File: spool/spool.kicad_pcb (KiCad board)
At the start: 4 copper layers, 80 x 95 mm, 135 parts, among them J1 USB_B_Micro, J13 Conn_02x10_Counter_Clockwise, J14 Conn_01x07, J2 SWD, J3 Switch_1, J4 Switch_1, J5 Switch_1, J6 Switch_2, J7 Conn_01x02, J8 Conn_01x08, M1 Motor_DC, Q1 AO3400A, Q101 Q_NMOS_GSD, Q2 2N7002, SW1 USB_BOOT, SW2 RESET, SW3 SW_Push_DPDT, SW4 SW_Coded_SH-7010, SW5 SW_Push_DPDT, U1 TPS63070RNMR, U10 HT75xx-1-SOT89, U101 MMA8451QR1, U102 INA219AxDCN, U103 DY-ITR8402, U104 DY-ITR8402, U11 TPL0401B-10-Q1, U12 BS612, U14 PCF8563T, U3 AS5600-ASOT, U6 DRV8871DDA, U7 W25Q128JVS, U8 RP2040, U9 BS612, Y1 Crystal_GND24, Y2 Crystal

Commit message: Tidy up
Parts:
- L101: footprint Connector_JST:JST_XA_B02B-XASK-1-A_1x02_P2.50mm_Vertical -> Connector_JST:JST_XA_B03B-XASK-1-A_1x03_P2.50mm_Vertical
- R103: value R_Shunt -> 100mΩ
- moved D101 6.75 mm to (-25.7, -30.6), turned to -90 degrees
- moved Q101 4.59 mm to (-16.7, -28.3)
- moved R104 2.62 mm to (31.4, -3.52)
- moved L101 1.91 mm to (-20.2, -38.3), turned to -90 degrees
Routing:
- net Net-(D101-A): track 6.80 -> 17.0 mm
- net SDA: track 118.9 -> 124.8 mm
- net +12V: track 27.4 -> 31.4 mm
- net RELEASE: track 68.9 -> 65.6 mm
- net SCL: track 122.7 -> 124.7 mm
- net GND: track 80.0 -> 78.1 mm, vias 79 -> 80
- net +3V3: track 61.3 -> 61.6 mm, vias 29 -> 47
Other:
- outline, holes or cut-outs redrawn
- board text added: "Magnet Release"
- board text added: "Motor"

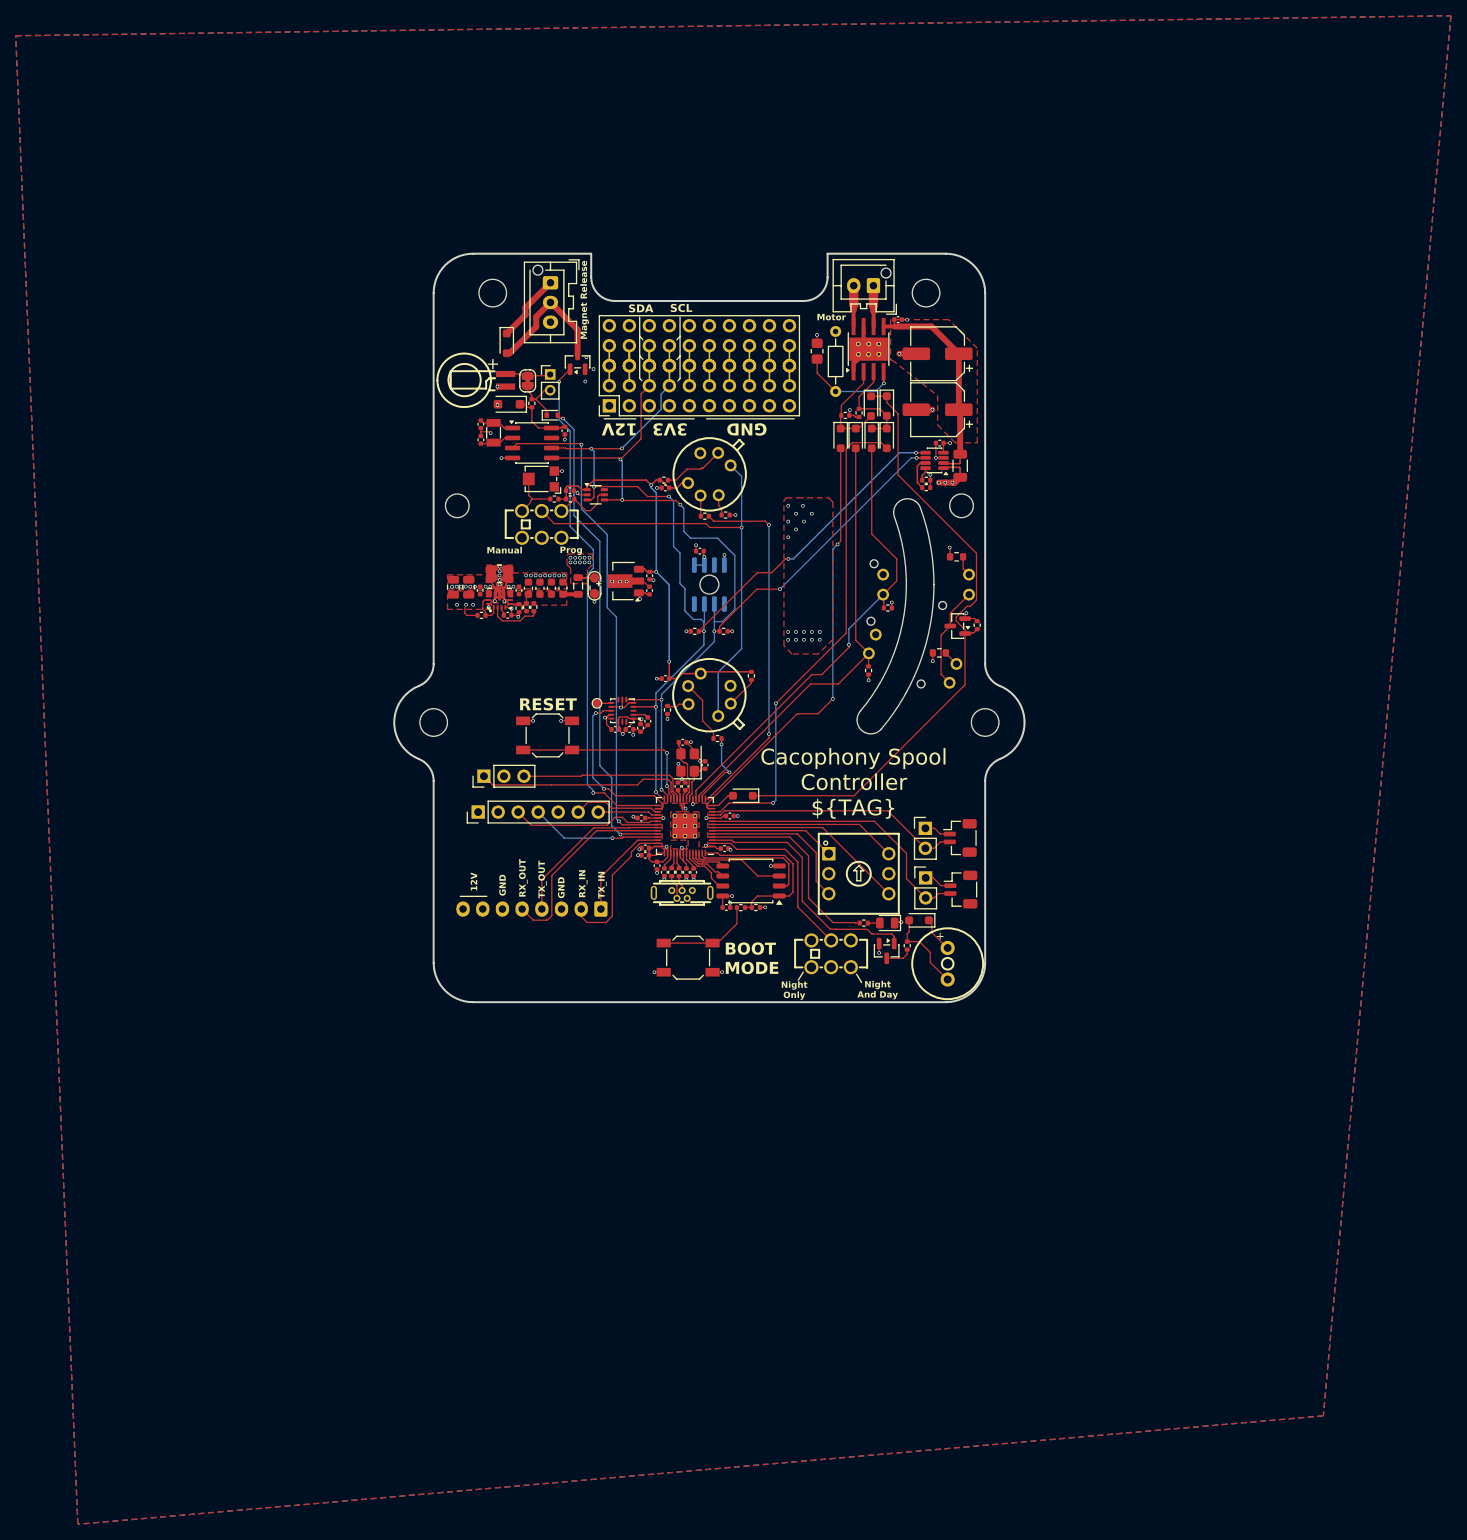
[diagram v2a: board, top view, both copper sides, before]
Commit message: Add servo, more inputs and update board layout
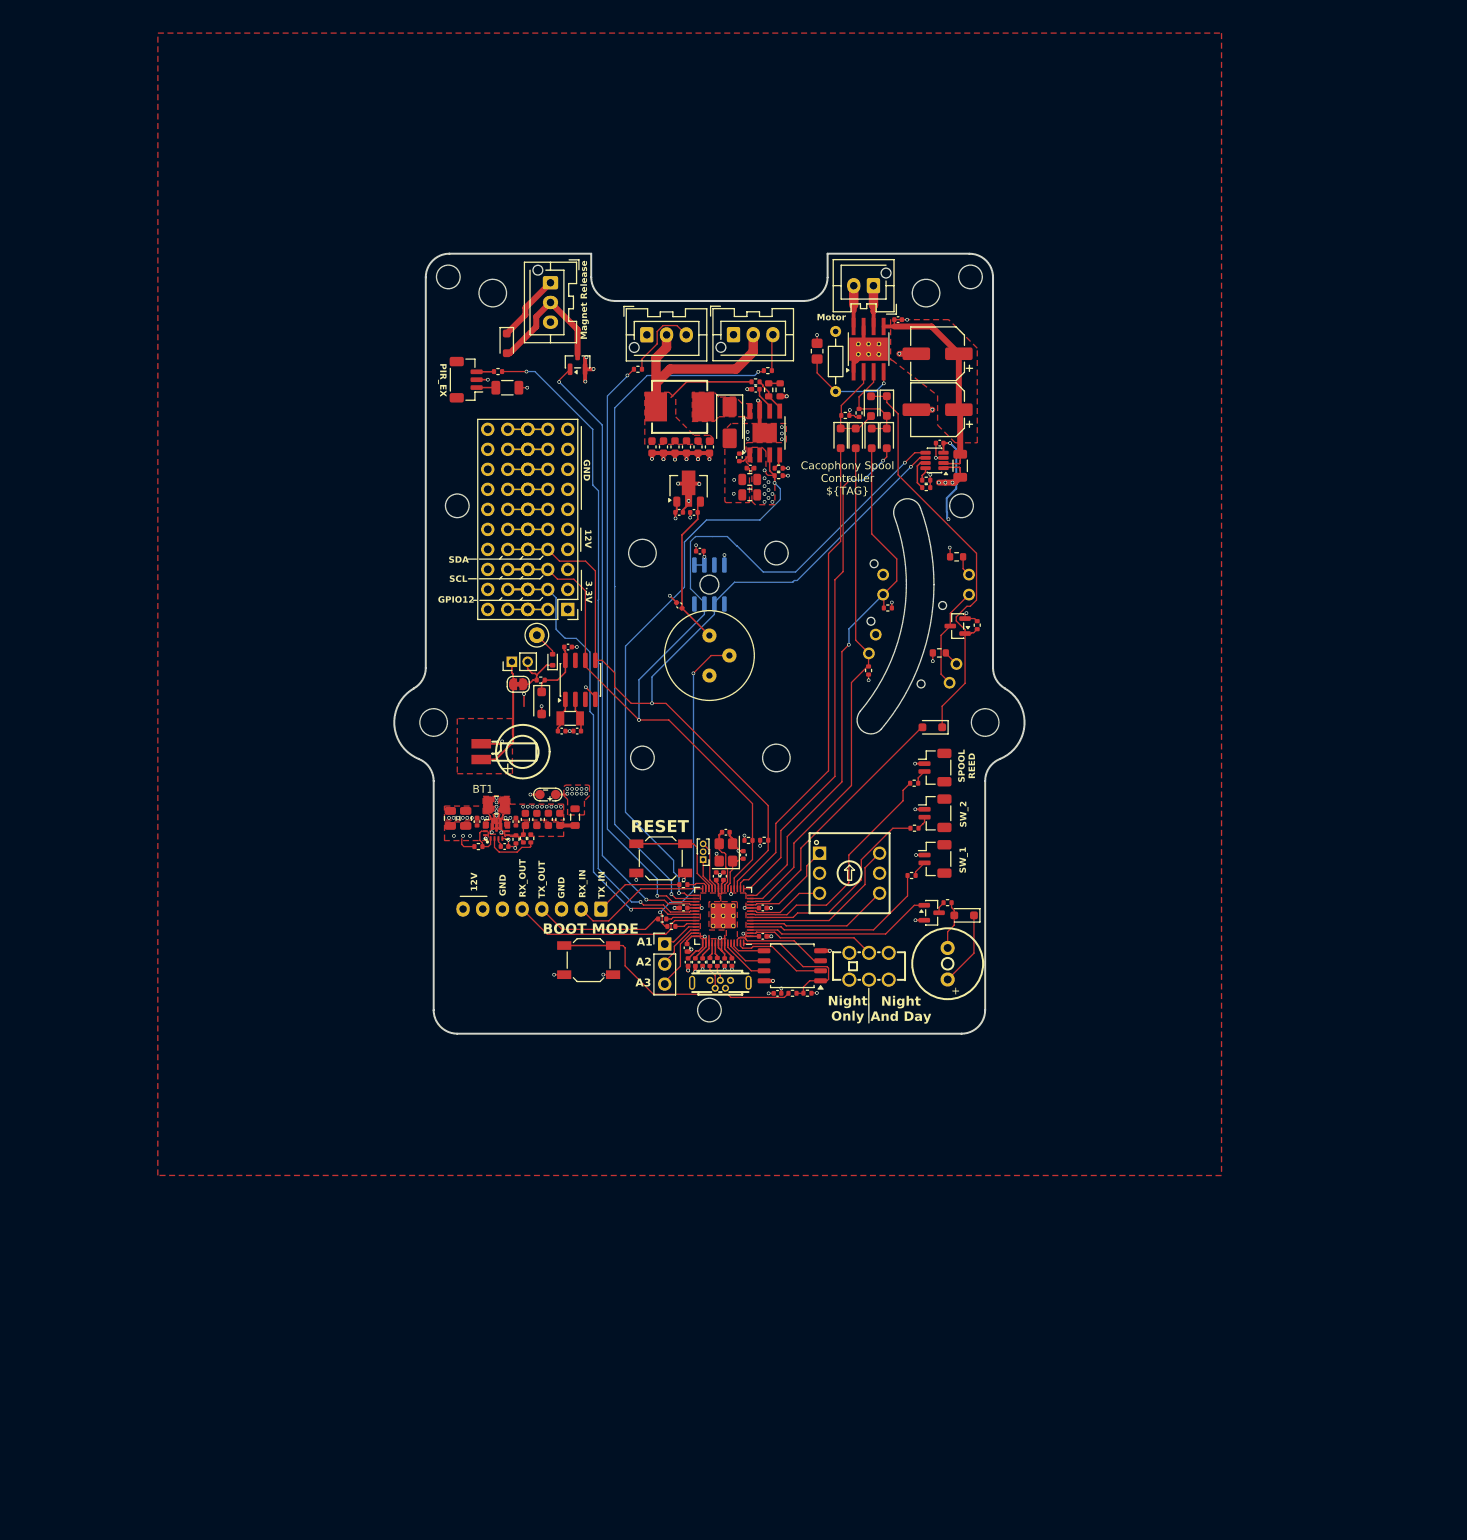
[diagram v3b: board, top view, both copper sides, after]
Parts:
- removed C101, C102: 100n, Capacitor_SMD:C_0402_1005Metric
- removed C103, C105: 2.2uF, Capacitor_SMD:C_0402_1005Metric
- removed D1: LED, LED_SMD:LED_0805_2012Metric
- removed J14: Conn_01x07, Connector_PinHeader_2.54mm:PinHeader_1x07_P2.54mm_Vertical
- removed R24, R30: 1k, Resistor_SMD:R_0402_1005Metric
- removed R28, R29: 10k, Resistor_SMD:R_0402_1005Metric
- removed RV1: 10k, Potentiometer_SMD:Potentiometer_Bourns_TC33X_Vertical
- removed SW3: SW_Push_DPDT, cacophony-library:SW-TH_K3-2235D-F1
- removed TP101: TestPoint, cacophony-library:TP_PAD
- removed U101: MMA8451QR1, cacophony-library:QFN-16_L3.0-W3.0-P0.50-TL_FXOS8700CQR1
- removed U11: TPL0401B-10-Q1, Package_TO_SOT_SMD:Texas_R-PDSO-G6
- removed U12: BS612, cacophony-library:SENSORM-TH_BS612
- added C36: 22uF, Capacitor_SMD:C_0603_1608Metric, F.Cu at (0.01, -17.5)
- added C37: 22nF, Capacitor_SMD:C_0402_1005Metric, F.Cu at (5.88, -24.8)
- added C38: 100nF, Capacitor_SMD:C_0402_1005Metric, F.Cu at (3.80, -16.1)
- added C40: 100n, Capacitor_SMD:C_0402_1005Metric, F.Cu at (-3.82, 2.64)
- added C46: 22uF, Capacitor_SMD:C_0603_1608Metric, F.Cu at (-1.45, -17.5)
- added C47: 22uF, Capacitor_SMD:C_0603_1608Metric, F.Cu at (-2.91, -17.5)
- added C48: 22uF, Capacitor_SMD:C_0603_1608Metric, F.Cu at (-4.37, -17.5)
- added C49: 22uF, Capacitor_SMD:C_0603_1608Metric, F.Cu at (-5.83, -17.5)
- added C50: 22uF, Capacitor_SMD:C_0603_1608Metric, F.Cu at (-7.29, -17.5)
- added D17: D_Shockley, Diode_SMD:D_SMA, F.Cu at (2.57, -20.6)
- added H10: MountingHole, cacophony-library:MountingHole_3.5mm_M3, F.Cu at (8.50, 22.0)
- added H11: MountingHole, cacophony-library:3.0mm_key_hole, F.Cu at (-33.1, -39.1)
- added H12: MountingHole, cacophony-library:3.0mm_key_hole, F.Cu at (33.1, -39.1)
- added H13: MountingHole, cacophony-library:3.0mm_key_hole, F.Cu at (0.00, 54.0)
- added H7: MountingHole, cacophony-library:3.0mm_key_hole, F.Cu at (-8.50, 22.0)
- added H8: MountingHole, cacophony-library:3.0mm_key_hole, F.Cu at (8.50, -4.00)
- added H9: MountingHole, cacophony-library:MountingHole_3.5mm_M3, F.Cu at (-8.50, -4.00)
- added J9: Switch_2, Connector_JST:JST_SH_BM02B-SRSS-TB_1x02-1MP_P1.00mm_Vertical, F.Cu at (28.6, 23.2)
- added L2: 4.7uH, cacophony-library:IND-SMD_L7.0-W6.6, F.Cu at (-3.78, -22.6)
- added M2: Servo, Connector_JST:JST_XA_B03B-XASK-1-A_1x03_P2.50mm_Vertical, F.Cu at (-7.94, -31.7)
- added M3: Servo, Connector_JST:JST_XA_B03B-XASK-1-A_1x03_P2.50mm_Vertical, F.Cu at (3.06, -31.7)
- added R34: 1k, Resistor_SMD:R_0402_1005Metric, F.Cu at (-9.07, -27.3)
- added R35: 1k, Resistor_SMD:R_0402_1005Metric, F.Cu at (7.42, -27.2)
- added R37: 1k, Resistor_SMD:R_0402_1005Metric, F.Cu at (-4.83, 43.4)
- added R38: 1k, Resistor_SMD:R_0402_1005Metric, F.Cu at (25.7, 36.9)
- added R39: 1k, Resistor_SMD:R_0402_1005Metric, F.Cu at (26.0, 25.2)
- added R40: 1k, Resistor_SMD:R_0402_1005Metric, F.Cu at (26.0, 30.9)
- added R41: 1k, Resistor_SMD:R_0402_1005Metric, F.Cu at (-26.8, -27.0)
- added R42: 1k, Resistor_SMD:R_1206_3216Metric, F.Cu at (-25.6, -25.0)
- added R43: 1k, Resistor_SMD:R_0402_1005Metric, F.Cu at (-5.99, 42.4)
- added R44: 1k, Resistor_SMD:R_0402_1005Metric, F.Cu at (-3.30, 38.1)
- added TP2: TestPoint, TestPoint:TestPoint_Loop_D1.80mm_Drill1.0mm_Beaded, F.Cu at (-21.9, 6.42)
- added U2: PA_PIR, cacophony-library:PA_PIR, F.Cu at (0.00, 9.00)
- C27: value 100n -> 2.2uF
- C28, C29: value 100n -> 22uF; footprint Capacitor_SMD:C_0402_1005Metric -> Capacitor_SMD:C_0805_2012Metric
- J2: footprint Connector_PinHeader_2.54mm:PinHeader_1x03_P2.54mm_Vertical -> Connector_PinHeader_1.00mm:PinHeader_1x03_P1.00mm_Vertical
- J3: value Switch_1 -> Conn_01x03; footprint Connector_PinHeader_2.54mm:PinHeader_1x02_P2.54mm_Vertical -> Connector_JST:JST_SH_BM03B-SRSS-TB_1x03-1MP_P1.00mm_Vertical
- J4, J6: footprint cacophony-library:JST_SH_BM02B-SRSS-TB_1x02-1MP_P1.00mm_Vertical -> Connector_JST:JST_SH_BM02B-SRSS-TB_1x02-1MP_P1.00mm_Vertical
- J5: value Switch_1 -> Conn_01x03; footprint Connector_PinHeader_2.54mm:PinHeader_1x02_P2.54mm_Vertical -> Connector_PinHeader_2.54mm:PinHeader_1x03_P2.54mm_Vertical
- L101: footprint Connector_JST:JST_XA_B03B-XASK-1-A_1x03_P2.50mm_Vertical -> cacophony-library:JST_XA_B03B_2_Pin
- R22: value 10k -> 47k
- R25: value 10k -> 100k
- R26: value 1k -> 560; footprint Resistor_SMD:R_0402_1005Metric -> Resistor_SMD:R_0603_1608Metric
- R27: value 10k -> 680; footprint Resistor_SMD:R_0402_1005Metric -> Resistor_SMD:R_0603_1608Metric
- SW1, SW2: footprint Button_Switch_SMD:SW_SPST_SKQG_WithStem -> cacophony-library:SW_SPST_SKQG_WithStem
- U9: value BS612 -> LMR14050S; footprint cacophony-library:SENSORM-TH_BS612 -> Package_SO:TI_SO-PowerPAD-8
- moved J3 86.0 mm to (-30.9, -26.0), turned to 90 degrees
- moved BT1 47.2 mm to (-28.8, 21.2), turned to 180 degrees
- moved R26 44.7 mm to (7.52, -24.7), turned to 90 degrees
- moved C31 40.3 mm to (-18.8, 18.6), turned to 0 degrees
- moved C32 38.9 mm to (-16.8, 18.6), turned to 180 degrees
- moved JP1 38.5 mm to (-24.3, 12.7), turned to 0 degrees
- moved D2 38.1 mm to (-21.3, 15.0), turned to -90 degrees
- moved Y2 37.5 mm to (-17.7, 17.0), turned to 0 degrees
- moved J7 36.8 mm to (-25.1, 9.79), turned to 90 degrees
- moved J5 36.2 mm to (-5.67, 45.6)
- moved R32 35.1 mm to (-21.4, 12.1), turned to 180 degrees
- moved U9 34.0 mm to (7.01, -19.2), turned to 90 degrees
- moved R25 32.9 mm to (8.79, -13.8), turned to 180 degrees
- moved D3 31.0 mm to (-19.9, 9.54), turned to 90 degrees
- moved U14 30.7 mm to (-16.4, 12.1), turned to 90 degrees
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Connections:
- C27 pad 1: +3V3_Lin -> +12V
- C28 pad 1: +3V3_Lin -> +12V
- C29 pad 1: +3V3_Lin -> +12V
- D3 pad 2: RTC_BAT_SENSE -> /RTC_BAT_SENSE
- D4 pad 2: Net-(D4-A) -> H_IN2
- D5 pad 2: Net-(D10-K) -> H_IN1
- D6 pad 2: Net-(D6-A) -> /EN_PHOTO_PHY
- D7 pad 1: Net-(D4-A) -> Net-(D7-K)
- D8 pad 1: Net-(D4-A) -> Net-(D7-K)
- J13 pad 1: +12V -> +3V3
- J13 pad 3: +12V -> +3V3
- J13 pad 4: unconnected-(J13-Pin_4-Pad4) -> GPIO_12
- J13 pad 6: SDA -> SCL
- J13 pad 7: +3V3 -> +12V
- J13 pad 8: SCL -> SDA
- J13 pad 9: +3V3 -> +12V
- J3 pad 1: GND -> /EX_PIR_POWER
- J3 pad 2: SWITCH_1 -> GND
- J5 pad 1: GND -> /ADC1
- J5 pad 2: SWITCH_2 -> /ADC2
- R10 pad 1: Net-(D10-K) -> H_IN1
- R12 pad 1: Net-(D4-A) -> H_IN2
- R22 pad 1: +3V3_Lin -> Net-(U9-RT/SYNC)
- R22 pad 2: Net-(U9-OEN) -> GND
- R23 pad 1: /PIR_SENS_POT_MANUAL -> +6V
- R23 pad 2: +3V3_Lin -> Net-(U9-FB)
- R25 pad 2: Net-(U9-ONTIME) -> EN_6V
- R26 pad 1: PIR_1 -> Net-(U9-FB)
- R26 pad 2: Net-(U9-REL) -> Net-(R26-Pad2)
- R27 pad 1: /PIR_SENS_POT_PROG -> Net-(R26-Pad2)
- R27 pad 2: +3V3_Lin -> GND
- U14 pad 3: ~{RTC_INT} -> unconnected-(U14-~{INT}-Pad3)
- U6 pad 2: Net-(D4-A) -> Net-(D7-K)
- U8 pad 11: SWITCH_2 -> R_ENC_1
- U8 pad 12: H_IN1 -> /EN_PHOTO_PHY
- U8 pad 13: H_IN2 -> PHOTO_RESET_OUT
- U8 pad 14: Net-(D6-A) -> PHOTO_HOME_OUT
- U8 pad 15: PIR_2 -> H_IN1
- U8 pad 16: PIR_1 -> H_IN2
- U8 pad 17: PHOTO_RESET_OUT -> SDA
- U8 pad 18: PHOTO_HOME_OUT -> SCL
- U8 pad 27: SDA -> /RP2040_TX_IN_PHY
- U8 pad 28: SCL -> RP2040_RX_IN
- U8 pad 29: RELEASE -> EN_6V
- U8 pad 30: Accel INT1 -> /SERVO_1_PHY
- U8 pad 31: GPIO_20 -> /SERVO_2_PHY
- U8 pad 32: GPIO_21 -> RELEASE
- U8 pad 34: GPIO_34 -> /PIR_EX_PHY
- U8 pad 35: ~{RTC_INT} -> GPIO_12
- U8 pad 36: RP2040_TX_OUT -> /RP2040_TX_OUT_PHY
- U8 pad 38: RTC_BAT_SENSE -> /APIR_PHY
- U8 pad 39: GPIO_27 -> /ADC1
- U8 pad 4: LED_1_PHY -> /SW_1_PHY
- U8 pad 40: RP2040_TX_IN -> /ADC2
- U8 pad 41: RP2040_RX_IN -> /ADC3
- U8 pad 5: R_ENC_4 -> R_ENC_2
- U8 pad 6: R_ENC_1 -> R_ENC_8
- U8 pad 7: R_ENC_2 -> /SW_2_PHY
- U8 pad 8: R_ENC_8 -> /SPOOL_REED_PHY
- U8 pad 9: SWITCH_1 -> R_ENC_4
- U9 pad 1: PIR_SENS_POT -> Net-(U9-Boot)
- U9 pad 2: Net-(U9-OEN) -> +12V
- U9 pad 3: GND -> EN_6V
- U9 pad 4: +3V3_Lin -> Net-(U9-RT/SYNC)
- U9 pad 5: Net-(U9-REL) -> Net-(U9-FB)
- U9 pad 6: Net-(U9-ONTIME) -> Net-(U9-SS)
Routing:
- net /SERVO_1_PHY: track 0.00 -> 88.9 mm, vias 0 -> 2
- net /PIR_EX_PHY: track 0.00 -> 85.4 mm, vias 0 -> 2
- net /SERVO_2_PHY: track 0.00 -> 76.1 mm, vias 0 -> 2
- net EN_6V: track 0.00 -> 73.4 mm, vias 0 -> 2
- net ~{RTC_INT}: track 64.0 -> 0.00 mm, vias 2 -> 0
- net RTC_BAT_SENSE: track 61.5 -> 0.00 mm, vias 2 -> 0
- net PIR_SENS_POT: track 59.9 -> 0.00 mm, vias 1 -> 0
- net GPIO_12: track 0.00 -> 54.5 mm, vias 0 -> 1
- net PIR_2: track 46.4 -> 0.00 mm, vias 2 -> 0
- net APIR: track 0.00 -> 40.8 mm, vias 0 -> 2
- net +6V: track 0.00 -> 39.9 mm
- net +3V3_Lin: track 58.2 -> 19.4 mm, vias 3 -> 0
- net SWITCH_1: track 36.4 -> 2.07 mm
- net /EN_PHOTO_PHY: track 0.00 -> 32.6 mm
- net SWITCH_2: track 32.7 -> 1.72 mm
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- added copper zone on F.Cu, net +6V
- added copper zone on F.Cu, net /SW_6V
- removed copper zone on B.Cu, net GND
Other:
- board size 80 x 95 mm -> 80 x 99 mm
- board text added: "3.3V"
- board text added: "A1"
- board text added: "A2"
- board text added: "A3"
- board text added: "GPIO12"
- board text added: "PIR_EX"
- board text added: "SPOOL REED"
- board text added: "SW_1"
- board text added: "SW_2"
- board text removed: "3V3"
- board text removed: "Manual"
- board text removed: "Prog"

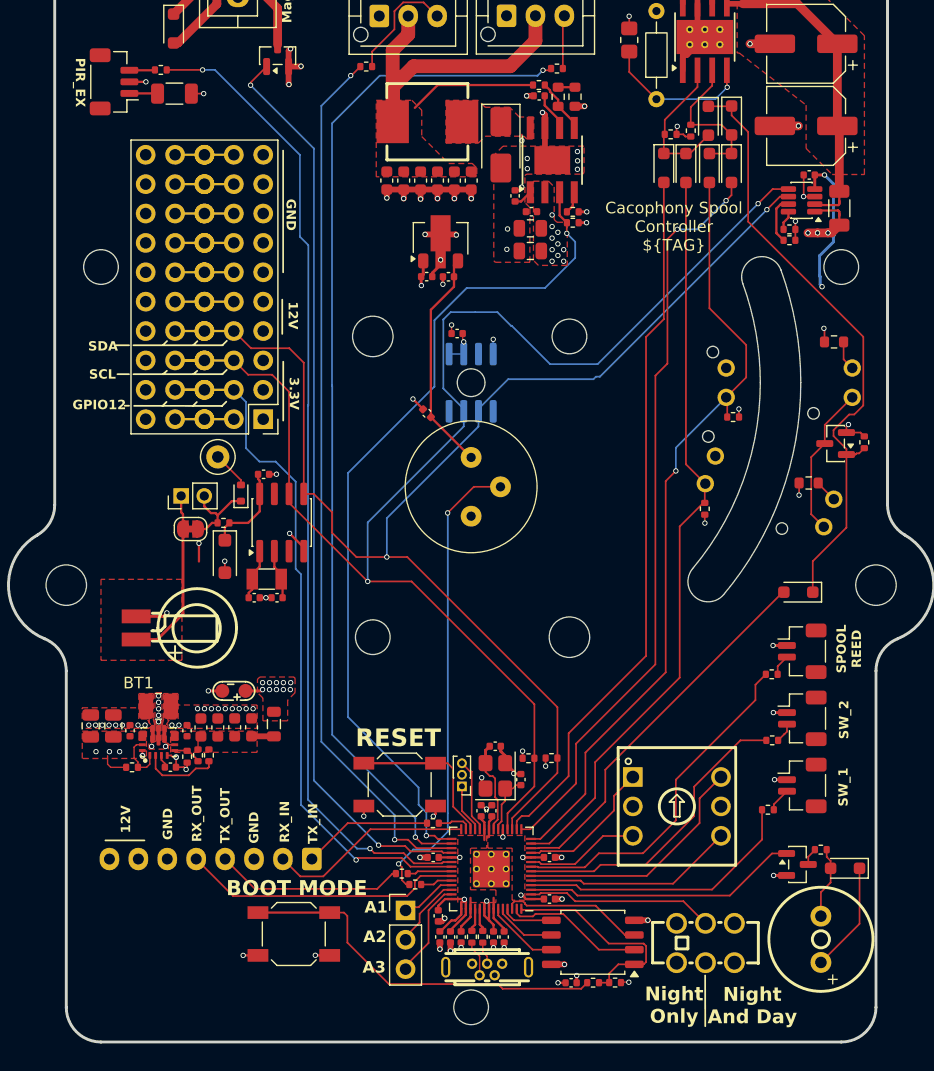
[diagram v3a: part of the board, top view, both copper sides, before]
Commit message: Update to use new PIR and added servo outputs
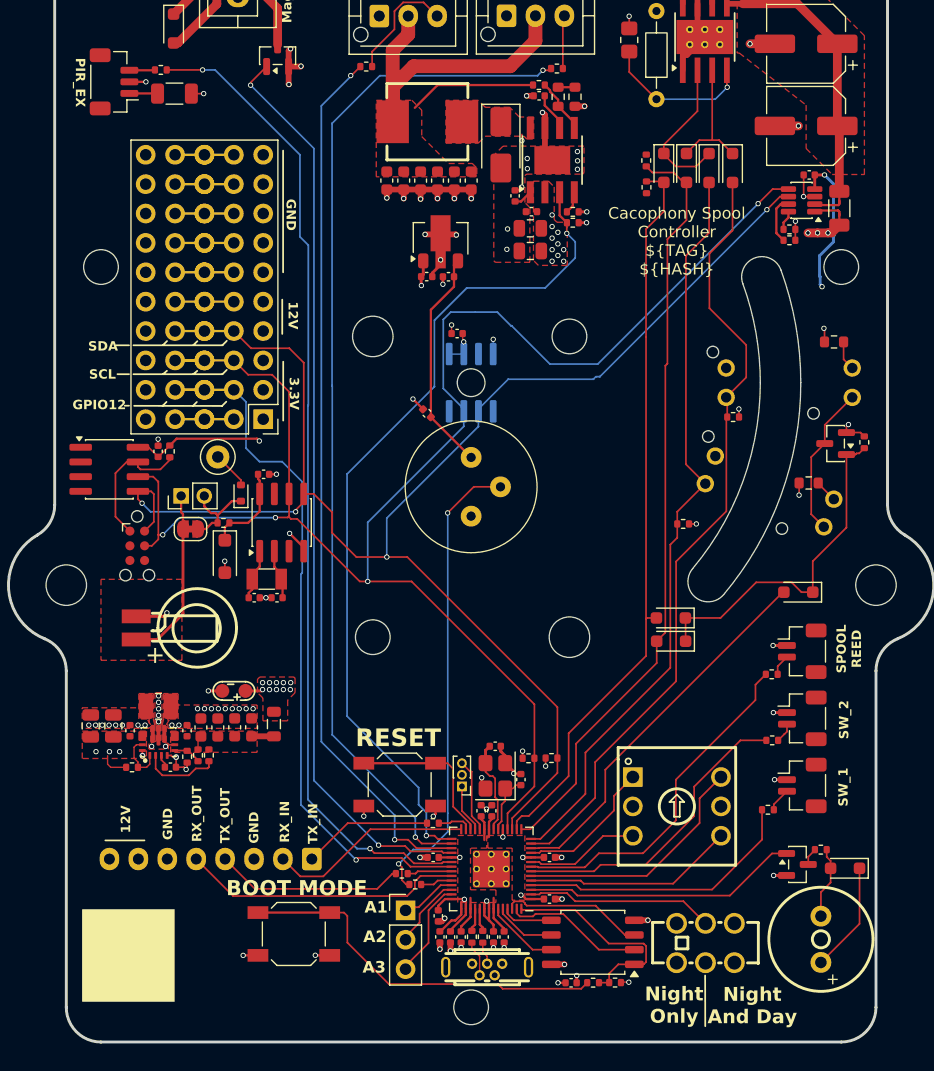
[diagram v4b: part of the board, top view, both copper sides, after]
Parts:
- added C39: 100n, Capacitor_SMD:C_0402_1005Metric, F.Cu at (-27.1, 5.93)
- added J1901: TC2030, cacophony-library:Tag-Connect_TC2030-IDC-NL_2x03_P1.27mm_Vertical, F.Cu at (-28.9, 14.1)
- added R115: 100k, Resistor_SMD:R_0402_1005Metric, F.Cu at (-26.1, 5.94)
- added U106: M24C02-WMN, Package_SO:SOIC-8_3.9x4.9mm_P1.27mm, F.Cu at (-31.3, 7.49)
- added U4: ~, cacophony-library:JLCPCB_QR_8mm, F.Cu at (-29.6, 49.5)
- moved D5 45.3 mm to (17.3, 22.4), turned to 180 degrees
- moved D4 43.1 mm to (17.3, 20.3), turned to 180 degrees
- moved R12 5.03 mm to (15.2, -16.9), turned to -90 degrees
- moved R10 4.63 mm to (15.1, -19.2), turned to 90 degrees
- moved D9 3.89 mm to (18.6, -18.6)
- moved R7 2.28 mm to (18.3, 12.2), turned to 180 degrees
- moved D10 2.00 mm to (22.6, -18.6)
- moved D7 2.00 mm to (20.6, -18.6)
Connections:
- U8 pad 13: PHOTO_RESET_OUT -> PHOTO_HOME_OUT
- U8 pad 14: PHOTO_HOME_OUT -> PHOTO_RESET_OUT
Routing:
- net EN_PHOTO: track 53.5 -> 29.5 mm
- net SDA: track 111.8 -> 133.4 mm, vias 2 -> 4
- net SCL: track 120.9 -> 141.9 mm, vias 2 -> 4
- net Net-(D7-K): track 0.00 -> 13.3 mm
- net EEPROM_~{WC}: track 0.00 -> 11.7 mm
- net +3V3: track 57.9 -> 69.4 mm, vias 28 -> 29
- net H_IN2: track 74.5 -> 64.0 mm
- net GND: track 91.1 -> 88.1 mm, vias 93 -> 92
- net Net-(D10-K): track 12.9 -> 11.0 mm
- net H_IN1: track 64.9 -> 66.3 mm, vias 2 -> 0
- net PHOTO_HOME_OUT: vias 1 -> 0
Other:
- board text added: "Cacophony Spool Controller ${TAG} ${HASH}"
- board text removed: "Cacophony Spool Controller ${TAG}"
